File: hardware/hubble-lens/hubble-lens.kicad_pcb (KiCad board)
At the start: 2 copper layers, 100 x 120 mm, 43 parts, among them J101 Left, J102 Bottom, J103 Right, J201 Power

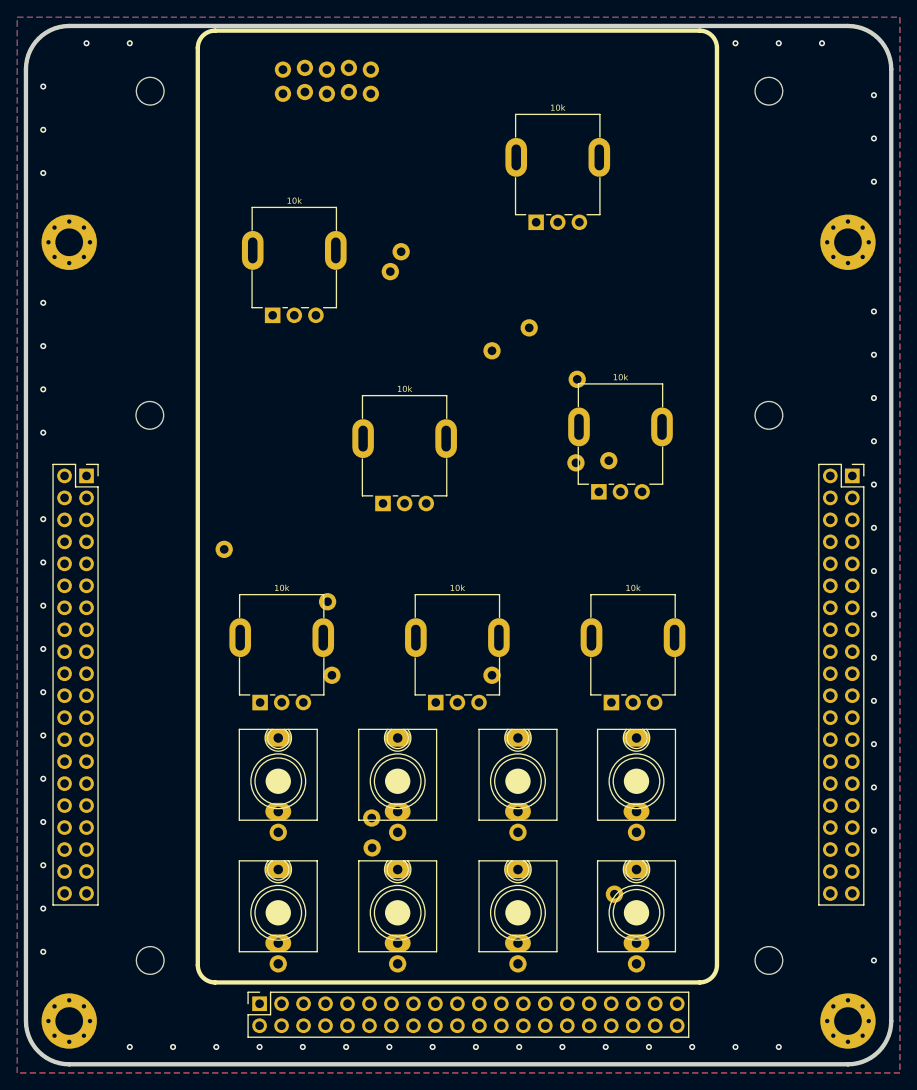
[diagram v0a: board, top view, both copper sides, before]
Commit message: Rough Draft of PCB for Hubble Lens
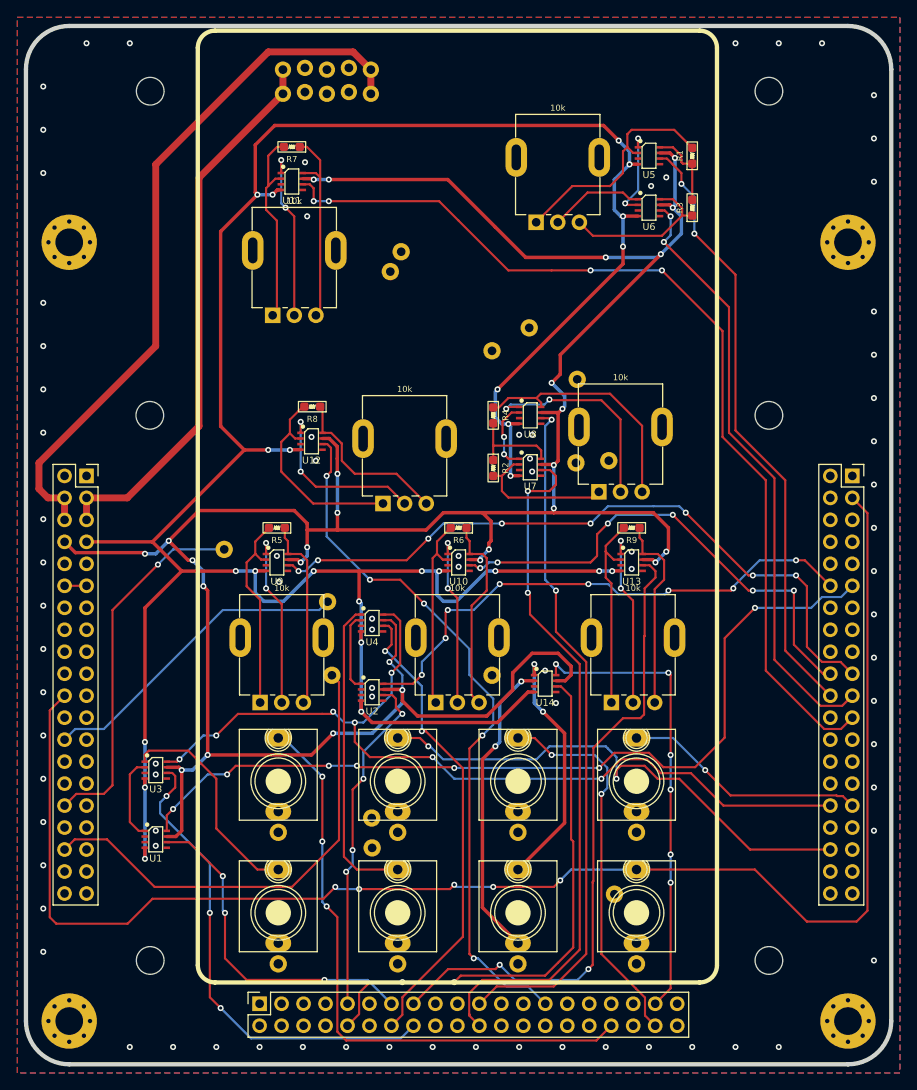
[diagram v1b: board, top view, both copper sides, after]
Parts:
- added R1: 5k, winterbloom:R_0603_HandSolder, F.Cu at (107.8, 64.7)
- added R2: 5k, winterbloom:R_0603_HandSolder, F.Cu at (84.8, 100.8)
- added R3: 5k, winterbloom:R_0603_HandSolder, F.Cu at (107.8, 70.7)
- added R4: 5k, winterbloom:R_0603_HandSolder, F.Cu at (84.8, 94.7)
- added R5: 10k, winterbloom:R_0603_HandSolder, F.Cu at (59.8, 107.7)
- added R6: 10k, winterbloom:R_0603_HandSolder, F.Cu at (80.8, 107.7)
- added R7: 10k, winterbloom:R_0603_HandSolder, F.Cu at (61.6, 63.7)
- added R8: 10k, winterbloom:R_0603_HandSolder, F.Cu at (63.9, 93.7)
- added R9: 10k, winterbloom:R_0603_HandSolder, F.Cu at (100.8, 107.7)
- added U1: DG449, winterbloom:Vishay_SOT-23_8, F.Cu at (45.8, 143.7)
- added U10: DG449, winterbloom:Vishay_SOT-23_8, F.Cu at (80.8, 111.7)
- added U11: DG449, winterbloom:Vishay_SOT-23_8, F.Cu at (61.6, 67.7)
- added U12: DG449, winterbloom:Vishay_SOT-23_8, F.Cu at (63.8, 97.7)
- added U13: DG449, winterbloom:Vishay_SOT-23_8, F.Cu at (100.8, 111.7)
- added U14: DG449, winterbloom:Vishay_SOT-23_8, F.Cu at (90.8, 125.7)
- added U2: DG449, winterbloom:Vishay_SOT-23_8, F.Cu at (70.8, 126.7)
- added U3: DG449, winterbloom:Vishay_SOT-23_8, F.Cu at (45.8, 135.7)
- added U4: DG449, winterbloom:Vishay_SOT-23_8, F.Cu at (70.8, 118.7)
- added U5: DG449, winterbloom:Vishay_SOT-23_8, F.Cu at (102.8, 64.7)
- added U6: DG449, winterbloom:Vishay_SOT-23_8, F.Cu at (102.8, 70.7)
- added U7: DG449, winterbloom:Vishay_SOT-23_8, F.Cu at (89.1, 100.7)
- added U8: DG449, winterbloom:Vishay_SOT-23_8, F.Cu at (89.1, 94.7)
- added U9: DG449, winterbloom:Vishay_SOT-23_8, F.Cu at (59.8, 111.7)
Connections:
- J101 pad 15: unconnected-(J101-Pin_15-Pad15) -> IO22
- J101 pad 16: unconnected-(J101-Pin_16-Pad16) -> IO23
- J101 pad 17: unconnected-(J101-Pin_17-Pad17) -> IO20
- J101 pad 18: unconnected-(J101-Pin_18-Pad18) -> IO21
- J101 pad 3: +12V -> +12V_SWITCHED
- J101 pad 4: -12V -> -12V_SWITCHED
- J101 pad 5: +12V -> +12V_SWITCHED
- J101 pad 6: -12V -> -12V_SWITCHED
- J101 pad 7: unconnected-(J101-Pin_7-Pad7) -> +12V
- J101 pad 8: unconnected-(J101-Pin_8-Pad8) -> -12V
- J102 pad 10: unconnected-(J102-Pin_10-Pad10) -> IO14
- J102 pad 13: unconnected-(J102-Pin_13-Pad13) -> IO11
- J102 pad 14: unconnected-(J102-Pin_14-Pad14) -> HP_IN_SWITCH_1
- J102 pad 15: unconnected-(J102-Pin_15-Pad15) -> FM2_SWITCH
- J102 pad 16: unconnected-(J102-Pin_16-Pad16) -> IO10
- J102 pad 21: unconnected-(J102-Pin_21-Pad21) -> FM1_SWITCH_1
- J102 pad 22: unconnected-(J102-Pin_22-Pad22) -> FM1_SWITCH_2
- J102 pad 23: unconnected-(J102-Pin_23-Pad23) -> SER4.1
- J102 pad 24: unconnected-(J102-Pin_24-Pad24) -> SER4.0
- J102 pad 25: unconnected-(J102-Pin_25-Pad25) -> SER4.3
- J102 pad 26: unconnected-(J102-Pin_26-Pad26) -> SER4.2
- J102 pad 27: unconnected-(J102-Pin_27-Pad27) -> IO6
- J102 pad 3: unconnected-(J102-Pin_3-Pad3) -> IO19
- J102 pad 4: unconnected-(J102-Pin_4-Pad4) -> GND
- J102 pad 5: unconnected-(J102-Pin_5-Pad5) -> IO17
- J102 pad 6: unconnected-(J102-Pin_6-Pad6) -> IO18
- J102 pad 7: unconnected-(J102-Pin_7-Pad7) -> IO15
- J102 pad 8: unconnected-(J102-Pin_8-Pad8) -> IO16
- J102 pad 9: unconnected-(J102-Pin_9-Pad9) -> HP_IN_SWITCH_2
- J103 pad 20: IO2 -> HP_VOL_SWITCH
- J103 pad 21: IO3 -> CUTOFF_SWITCH_1
- J103 pad 22: IO4 -> CUTOFF_SWITCH_2
- J103 pad 25: unconnected-(J103-Pin_25-Pad25) -> SER1.3
- J103 pad 26: unconnected-(J103-Pin_26-Pad26) -> SER1.2
- J103 pad 27: unconnected-(J103-Pin_27-Pad27) -> SER1.1
- J103 pad 28: unconnected-(J103-Pin_28-Pad28) -> SER1.0
- J103 pad 3: EXT_OSC_A -> ADC_1A
- J201 pad 1: Net-(J201--12V-Pad1) -> -12V_SWITCHED
- J201 pad 10: Net-(J201-+12V-Pad10) -> +12V_SWITCHED
- J201 pad 2: Net-(J201--12V-Pad1) -> -12V_SWITCHED
- J201 pad 3: Net-(J201-GND-Pad3) -> GND
- J201 pad 4: Net-(J201-GND-Pad3) -> GND
- J201 pad 5: Net-(J201-GND-Pad3) -> GND
- J201 pad 6: Net-(J201-GND-Pad3) -> GND
- J201 pad 7: Net-(J201-GND-Pad3) -> GND
- J201 pad 8: Net-(J201-GND-Pad3) -> GND
- J201 pad 9: Net-(J201-+12V-Pad10) -> +12V_SWITCHED
- J301 pad T: unconnected-(J301-Tip-PadT) -> LP_IN
- J302 pad T: unconnected-(J302-Tip-PadT) -> HP_IN
- J401 pad T: unconnected-(J401-Tip-PadT) -> DAC_2A
- J402 pad T: unconnected-(J402-Tip-PadT) -> DAC_1B
- J601 pad T: unconnected-(J601-Tip-PadT) -> DAC_3A
- J701 pad T: unconnected-(J701-Tip-PadT) -> DAC_4A
- J801 pad T: unconnected-(J801-Tip-PadT) -> Net-(J801-Tip)
- J801 pad TN: unconnected-(J801-Tip_normalize-PadTN) -> Net-(J801-Tip_normalize)
- J802 pad T: unconnected-(J802-Tip-PadT) -> ADC_1A
- RV301 pad 1: unconnected-(RV301-Pad1) -> /Knob Multiplexers/LP_VOL_PIN_1
- RV301 pad 2: unconnected-(RV301-Pad2) -> /Knob Multiplexers/LP_VOL_PIN_2
- RV301 pad 3: unconnected-(RV301-Pad3) -> /Knob Multiplexers/LP_VOL_PIN_3
- RV302 pad 1: unconnected-(RV302-Pad1) -> /Knob Multiplexers/HP_VOL_PIN_1
- RV302 pad 2: unconnected-(RV302-Pad2) -> /Knob Multiplexers/HP_VOL_PIN_2
- RV302 pad 3: unconnected-(RV302-Pad3) -> /Knob Multiplexers/HP_VOL_PIN_3
- RV401 pad 1: unconnected-(RV401-Pad1) -> /Knob Multiplexers/CUTOFF_PIN_1
- RV401 pad 2: unconnected-(RV401-Pad2) -> /Knob Multiplexers/CUTOFF_PIN_2
- RV401 pad 3: unconnected-(RV401-Pad3) -> /Knob Multiplexers/CUTOFF_PIN_3
- RV402 pad 1: unconnected-(RV402-Pad1) -> /Knob Multiplexers/FM1_PIN_1
- RV402 pad 2: unconnected-(RV402-Pad2) -> /Knob Multiplexers/FM1_PIN_2
- RV402 pad 3: unconnected-(RV402-Pad3) -> /Knob Multiplexers/FM1_PIN_3
- RV403 pad 1: unconnected-(RV403-Pad1) -> /Knob Multiplexers/FM2_PIN_1
- RV403 pad 2: unconnected-(RV403-Pad2) -> /Knob Multiplexers/FM2_PIN_2
- RV403 pad 3: unconnected-(RV403-Pad3) -> /Knob Multiplexers/FM2_PIN_3
- RV601 pad 1: unconnected-(RV601-Pad1) -> /Knob Multiplexers/RESO_PIN_1
- RV601 pad 2: unconnected-(RV601-Pad2) -> /Knob Multiplexers/RESO_PIN_2
- RV601 pad 3: unconnected-(RV601-Pad3) -> /Knob Multiplexers/RESO_PIN_3
- RV701 pad 1: unconnected-(RV701-Pad1) -> /Knob Multiplexers/SALT_PIN_1
- RV701 pad 2: unconnected-(RV701-Pad2) -> /Knob Multiplexers/SALT_PIN_2
- RV701 pad 3: unconnected-(RV701-Pad3) -> /Knob Multiplexers/SALT_PIN_3
- TP201 pad 1: unconnected-(TP201-Pad1) -> ADC_2A
- TP202 pad 1: unconnected-(TP202-Pad1) -> ADC_3A
- TP203 pad 1: unconnected-(TP203-Pad1) -> ADC_4A
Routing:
- net -12V: track 0.00 -> 317.6 mm, vias 0 -> 27
- net +12V: track 0.00 -> 312.0 mm, vias 0 -> 25
- net ADC_1A: track 0.00 -> 175.6 mm, vias 0 -> 5
- net IO5: track 0.00 -> 111.1 mm, vias 0 -> 4
- net DAC_1A: track 0.00 -> 103.5 mm, vias 0 -> 7
- net EXT_FG_A: track 0.00 -> 100.3 mm, vias 0 -> 7
- net -12V_SWITCHED: track 0.00 -> 82.9 mm
- net IO6: track 0.00 -> 82.2 mm, vias 0 -> 5
- net FM1_SWITCH_2: track 0.00 -> 81.1 mm, vias 0 -> 2
- net IO1: track 0.00 -> 80.7 mm, vias 0 -> 8
- net FM1_SWITCH_1: track 0.00 -> 80.0 mm, vias 0 -> 2
- net FM2_SWITCH: track 0.00 -> 75.5 mm, vias 0 -> 2
- net CUTOFF_SWITCH_2: track 0.00 -> 70.7 mm, vias 0 -> 2
- net CUTOFF_SWITCH_1: track 0.00 -> 70.1 mm, vias 0 -> 2
- net DAC_3A: track 0.00 -> 69.9 mm, vias 0 -> 3
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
